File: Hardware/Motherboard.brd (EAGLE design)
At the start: 124.5 x 73.7 mm, 92 parts, among them J1 MICROMOD-2222-C, J10 MICRO-SD-PUSH-PUSH-EXT-PIN, J2 Vertical Qwiic Connector, J4 QWIIC_RIGHT_ANGLE, J5 CORTEX_JTAG_DEBUG_MINIMUM_PTH, J6 MICROMOD_CARRIER, J7 MICROMOD_CARRIER, Q1 3.1A/30V/105mΩ, U2 MCP73831, U5 AP7361C-33

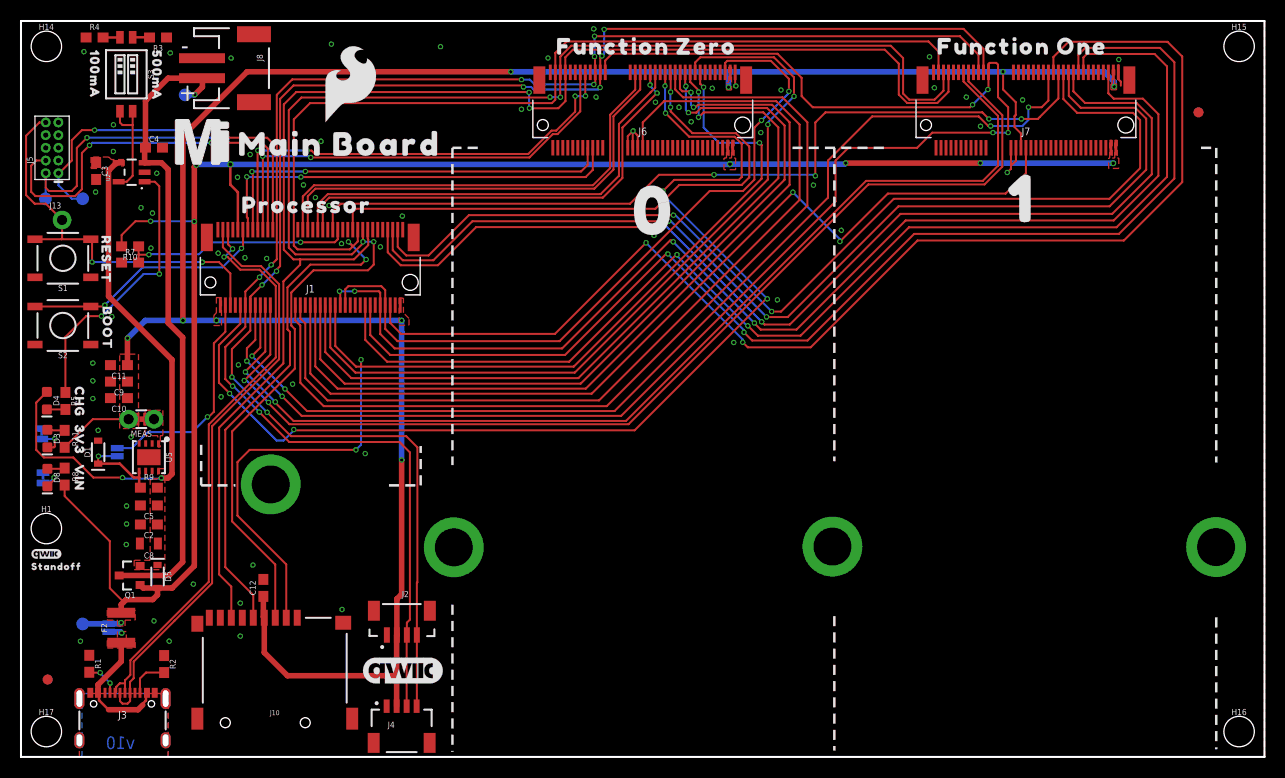
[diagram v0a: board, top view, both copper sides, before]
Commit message: Adds 10k pull down to PCHAN MOSFET
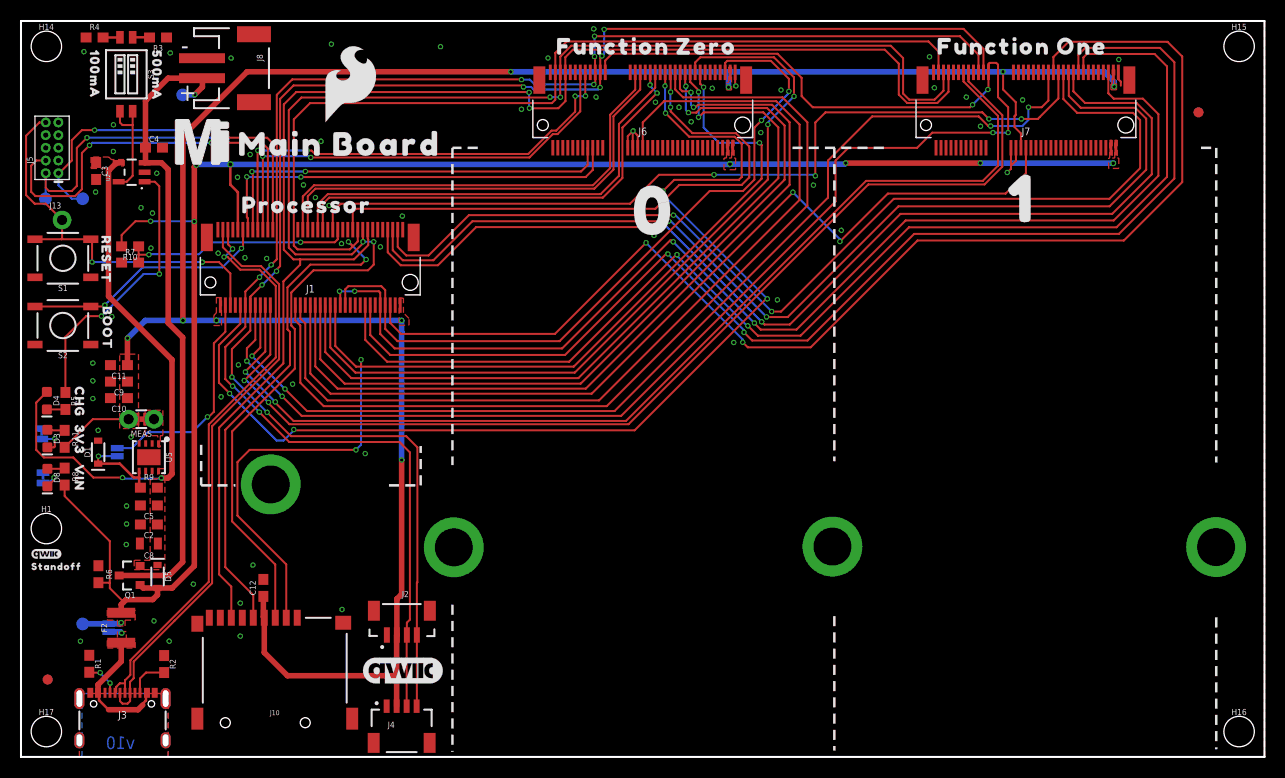
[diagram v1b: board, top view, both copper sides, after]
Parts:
- added R6: 10k, SparkFun-Resistors:0603
- moved TP3 0.25 mm to (16.2, 66.3)
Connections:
- net GND: now also R6.1
- net VIN: now also R6.2
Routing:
- net VIN: track 178.0 -> 179.2 mm
- net GND: track 13.7 -> 13.0 mm
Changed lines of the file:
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@@
 </element>
 <element name="TP2" library="SparkFun-Connectors" package="PAD.03X.05" value="TEST-POINT3X5" x="6.173" y="55.868" smashed="yes" rot="MR180"/>
-<element name="TP3" library="SparkFun-Connectors" package="PAD.03X.05" value="TEST-POINT3X5" x="16.4338" y="66.2686" smashed="yes" rot="MR270"/>
+<element name="TP3" library="SparkFun-Connectors" package="PAD.03X.05" value="TEST-POINT3X5" x="16.1798" y="66.2686" smashed="yes" rot="MR270"/>
 <element name="TP4" library="SparkFun-Connectors" package="PAD.03X.05" value="TEST-POINT3X5" x="6.1722" y="13.3096" smashed="yes" rot="MR0"/>
 <element name="TP1" library="SparkFun-Connectors" package="PAD.03X.05" value="TEST-POINT3X5" x="2.444" y="55.858" smashed="yes" rot="MR0"/>
@@
 <element name="U$23" library="top" package="STANDOFF501" value="" x="3.556" y="19.05" smashed="yes"/>
 <element name="U$24" library="SparkFun-Aesthetics" package="SFE_LOGO_FLAME_.3" value="" x="33.02" y="67.31" smashed="yes"/>
+<element name="R6" library="SparkFun-Resistors" package="0603" value="10k" x="7.747" y="18.288" smashed="yes" rot="R270">
+<attribute name="NAME" x="8.509" y="18.288" size="0.6096" layer="25" font="vector" ratio="20" rot="R270" align="bottom-center"/>
+<attribute name="PROD_ID" value="RES-00824" x="7.747" y="18.288" size="1.778" layer="27" font="vector" ratio="15" rot="R270" display="off"/>
+<attribute name="VALUE" x="6.985" y="18.288" size="0.6096" layer="27" font="vector" ratio="20" rot="R270" align="top-center"/>
+</element>
 </elements>
 <signals>
@@
 <via x="10.5664" y="23.3172" extent="1-16" drill="0.3048"/>
 <via x="10.541" y="21.2598" extent="1-16" drill="0.3048"/>
-<wire x1="109.834" y1="68.521" x2="109.834" y2="69.2448" width="0.2032" layer="1"/>
 <wire x1="109.834" y1="68.521" x2="109.834" y2="67.839" width="0.2032" layer="1"/>
 <wire x1="110.0836" y1="67.5894" x2="110.0836" y2="67.183" width="0.2032" layer="1"/>
@@
 <via x="13.3096" y="13.6144" extent="1-16" drill="0.3048"/>
 <via x="17.2466" y="17.2974" extent="1-16" drill="0.3048"/>
+<contactref element="R6" pad="1"/>
 </signal>
 <signal name="V_BATT" class="1">
@@
 <wire x1="16.1798" y1="41.9862" x2="14.732" y2="43.434" width="0.5588" layer="1"/>
 <wire x1="14.732" y1="43.434" x2="14.732" y2="58.801" width="0.5588" layer="1"/>
-<wire x1="12.3745" y1="59.4716" x2="12.3745" y2="60.8655" width="0.5588" layer="1"/>
 <wire x1="14.7226" y1="67.9356" x2="18.1186" y2="67.9356" width="0.5588" layer="1"/>
-<wire x1="12.4596" y1="60.9854" x2="12.4596" y2="65.6726" width="0.5588" layer="1"/>
-<wire x1="12.4596" y1="65.6726" x2="14.7226" y2="67.9356" width="0.5588" layer="1"/>
-<wire x1="16.4338" y1="66.2686" x2="17.3736" y2="66.2686" width="0.5588" layer="16"/>
+<wire x1="14.7226" y1="67.9356" x2="12.4596" y2="65.6726" width="0.5588" layer="1"/>
+<wire x1="16.1798" y1="66.2686" x2="17.3736" y2="66.2686" width="0.5588" layer="16"/>
 <wire x1="17.3736" y1="66.2686" x2="17.399" y2="66.294" width="0.5588" layer="16"/>
 <via x="17.399" y="66.294" extent="1-16" drill="0.3048"/>
@@
 <contactref element="Q1" pad="3"/>
 <wire x1="14.8336" y1="18.161" x2="9.822" y2="18.161" width="0.5588" layer="1"/>
-<wire x1="12.3745" y1="60.8655" x2="12.4596" y2="60.9854" width="0" layer="19" extent="1-1"/>
+<wire x1="12.4596" y1="65.6726" x2="12.4596" y2="60.9854" width="0.5588" layer="1"/>
+<wire x1="12.4596" y1="60.9854" x2="12.4596" y2="59.5567" width="0.5588" layer="1"/>
+<wire x1="12.4596" y1="59.5567" x2="12.3745" y2="59.4716" width="0.5588" layer="1"/>
 </signal>
 <signal name="N$14">
@@
 <wire x1="4.3688" y1="26.1112" x2="8.89" y2="21.59" width="0.2032" layer="1"/>
 <wire x1="8.89" y1="16.891" x2="10.2769" y2="15.5041" width="0.2032" layer="1"/>
-<wire x1="8.89" y1="21.59" x2="8.89" y2="16.891" width="0.2032" layer="1"/>
+<wire x1="8.89" y1="21.59" x2="8.89" y2="17.399" width="0.2032" layer="1"/>
 <contactref element="TP4" pad="1"/>
+<wire x1="8.89" y1="16.891" x2="8.89" y2="17.399" width="0.2032" layer="1"/>
 <wire x1="8.763" y1="13.335" x2="6.1976" y2="13.335" width="0.5588" layer="16"/>
 <wire x1="6.1976" y1="13.335" x2="6.1722" y2="13.3096" width="0.5588" layer="16"/>
@@
 <wire x1="13.6652" y1="16.9094" x2="12.2236" y2="16.9094" width="0.5588" layer="1"/>
 <wire x1="12.2236" y1="16.9094" x2="11.922" y2="17.211" width="0.5588" layer="1"/>
+<contactref element="R6" pad="2"/>
+<wire x1="7.747" y1="17.438" x2="8.851" y2="17.438" width="0.2032" layer="1"/>
+<wire x1="8.851" y1="17.438" x2="8.89" y2="17.399" width="0.2032" layer="1"/>
 </signal>
 <signal name="SHLD">

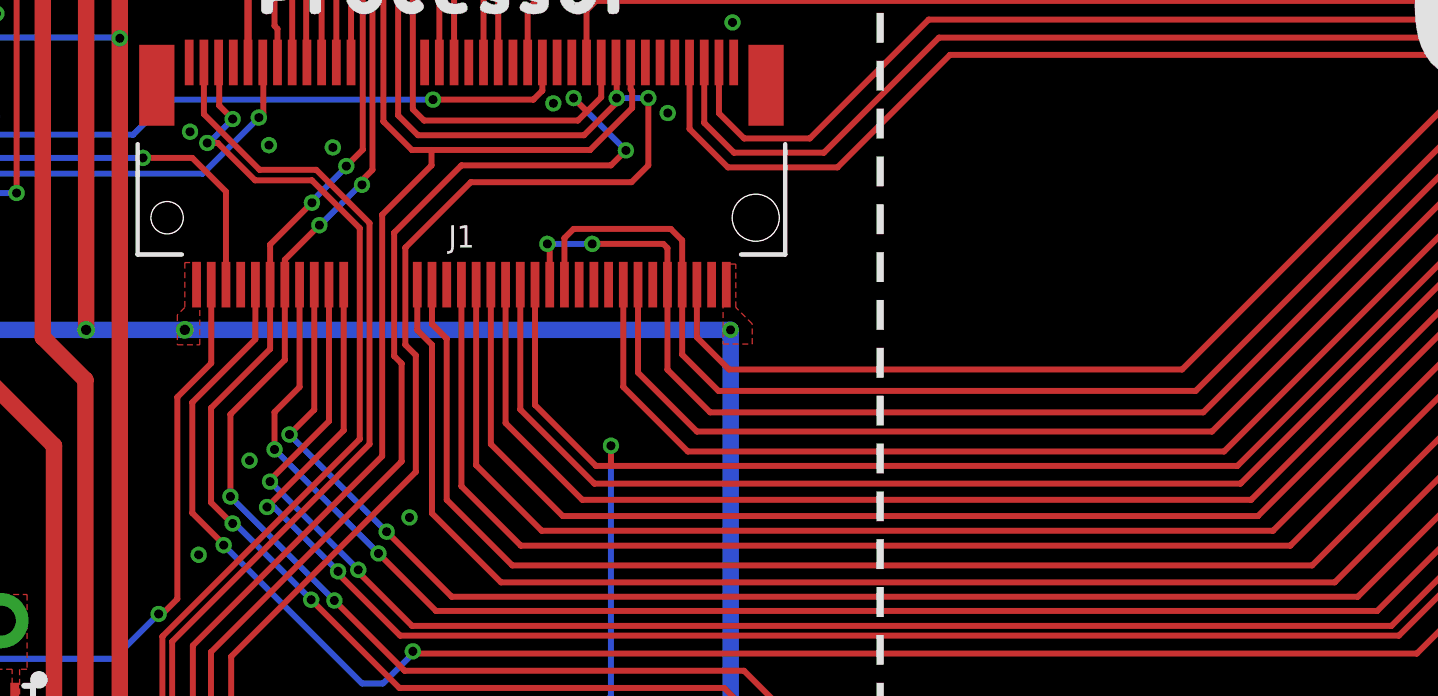
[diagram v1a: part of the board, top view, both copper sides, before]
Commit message: Adds jumpers to route power enable pins to G0/G1 for processors that don't have those nets routed
* Adds silk to added jumpers
* Adds PROD-ID to function board connectors
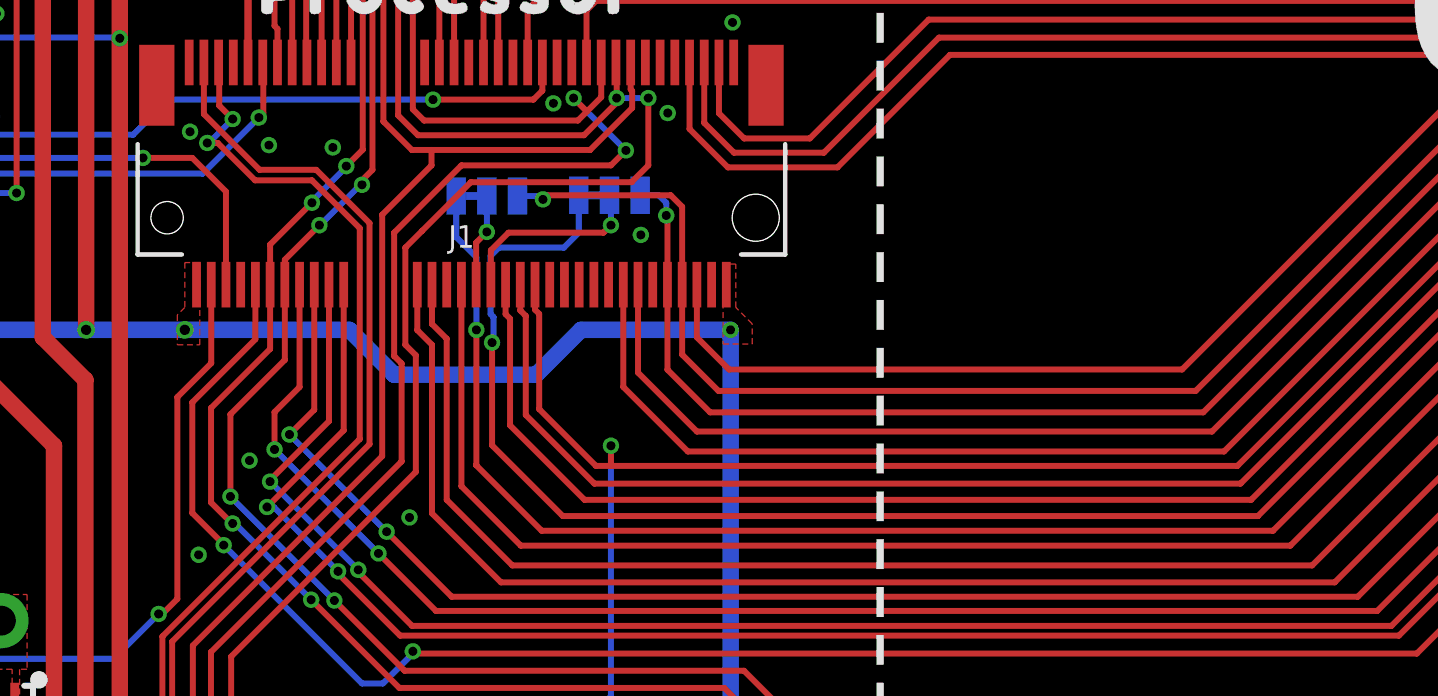
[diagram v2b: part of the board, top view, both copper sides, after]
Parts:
- added JP1, JP2: JUMPER-SMT_3_1-NC_TRACE_SILK, SparkFun-Jumpers:SMT-JUMPER_3_1-NC_TRACE_SILK
- added U$25: (no value), top:#G1#PROCESSOR#517
- added U$26: (no value), top:#G0#PROCESSOR#517
- added U$27: (no value), top:#ALT_PWR_EN1#517
- added U$28: (no value), top:#ALT_PWR_EN0#517
- H2, H3, H4, H8: value STAND-OFF-REFLOW2.5MM_TALL -> STAND-OFF-REFLOW-M2.5_2.5MM_TALL
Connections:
- new net G0-JUMPER: J1.40, JP2.2
- new net G1-JUMPER: J1.42, JP1.2
- net G0-PROCESSOR: now also JP2.3; no longer J1.40
- net G1-PROCESSOR: now also JP1.3; no longer J1.42
- net PWR_EN0: now also JP2.1; no longer J1.52
- net PWR_EN1: now also JP1.1; no longer J1.50
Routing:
- net G1-JUMPER: track 0.00 -> 6.64 mm, vias 0 -> 1
- net G1-PROCESSOR: track 81.5 -> 87.1 mm, vias 2 -> 3
- net G0-PROCESSOR: track 84.2 -> 87.9 mm, vias 2 -> 3
- net G0-JUMPER: track 0.00 -> 3.16 mm, vias 0 -> 1
- net PWR_EN1: track 116.9 -> 113.9 mm, vias 4 -> 3
- net 3.3V: track 242.4 -> 243.7 mm
- net PWR_EN0: track 73.6 -> 74.7 mm, vias 2 -> 3
- net GND: vias 72 -> 73

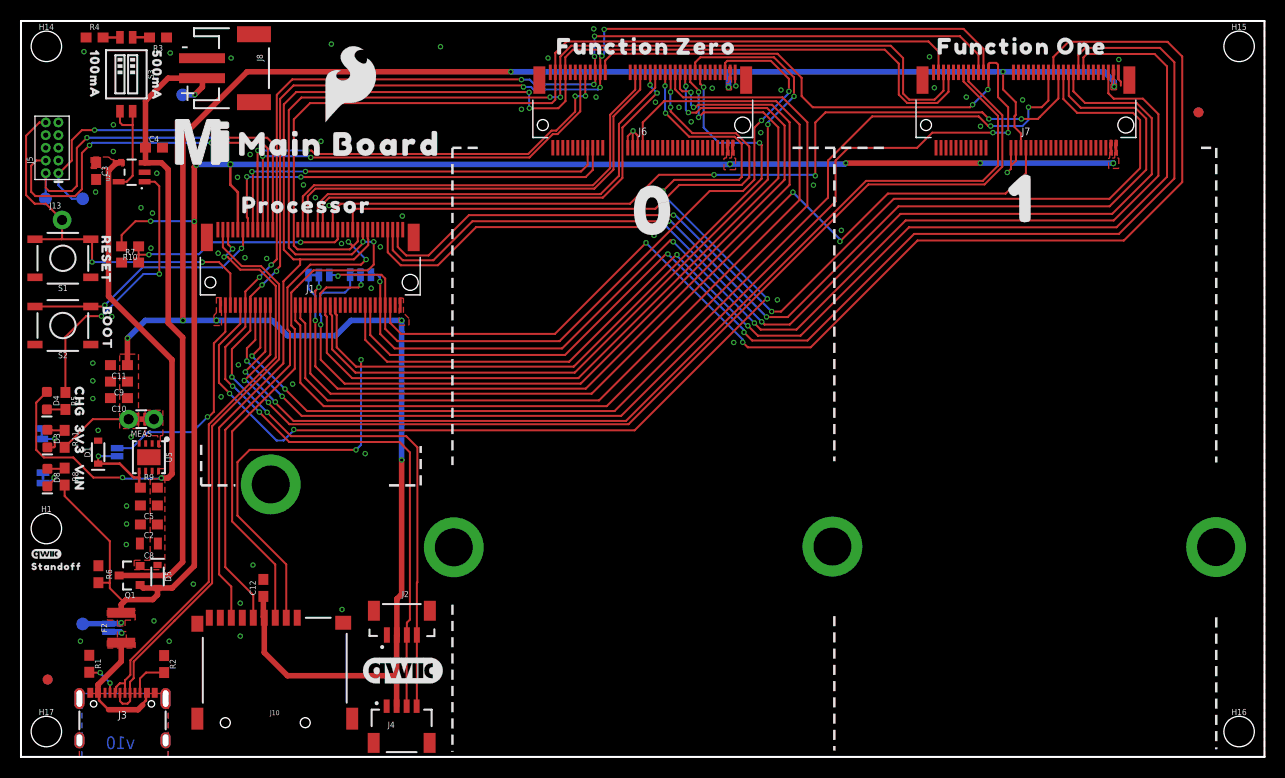
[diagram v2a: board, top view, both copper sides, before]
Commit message: Recreates changes from last change but instead moves jumpers to nets G5/G6
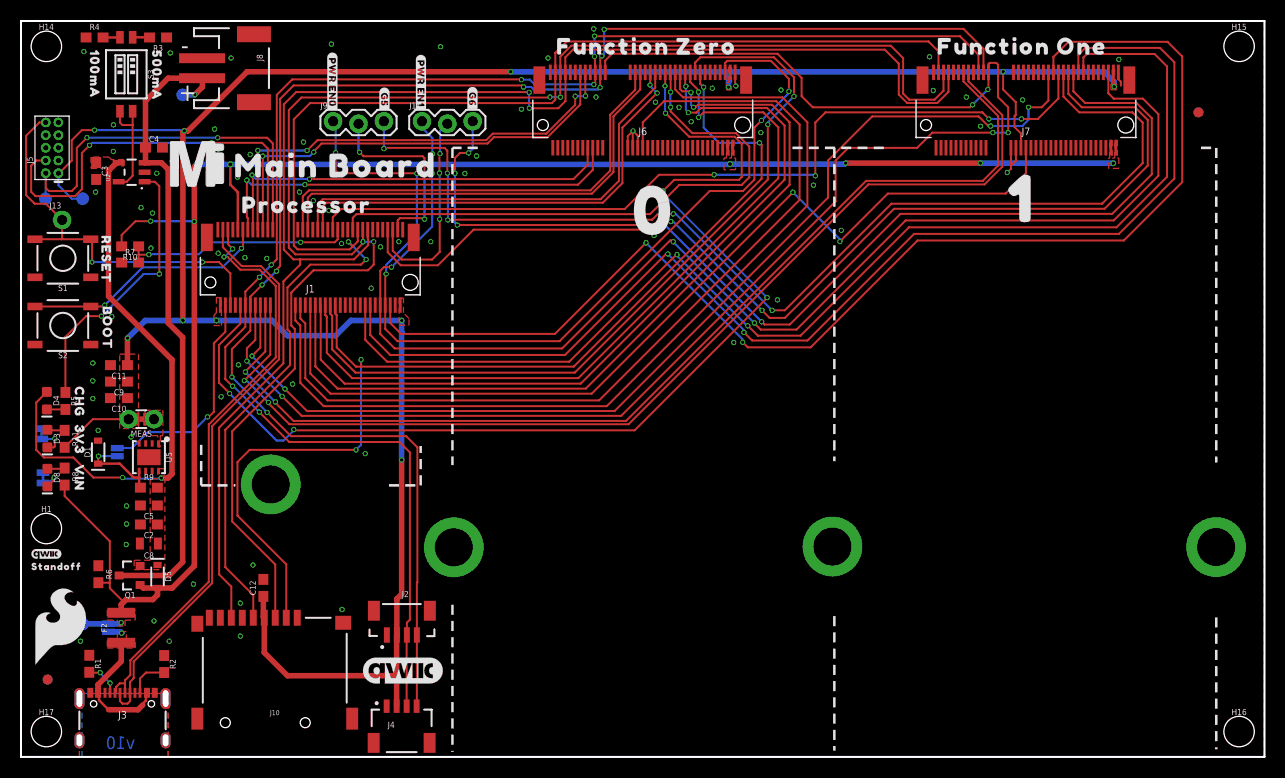
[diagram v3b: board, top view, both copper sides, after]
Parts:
- removed JP1, JP2: JUMPER-SMT_3_1-NC_TRACE_SILK, SparkFun-Jumpers:SMT-JUMPER_3_1-NC_TRACE_SILK
- added J11, J9: (no value), SparkFun-Connectors:1X03_LOCK
- added U$29: (no value), top:#G6#517
- added U$30: (no value), top:#PWR_EN0#517
- added U$31: (no value), top:#PWR_EN1#517
- added U$32: (no value), top:#G5#517
- moved U$24 61.6 mm to (3.99, 13.0)
- moved U$14 2.27 mm to (17.7, 59.4)
- moved U$21 2.19 mm to (31.5, 59.2)
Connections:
- removed net G0-JUMPER: J1.40, JP2.2
- removed net G1-JUMPER: J1.42, JP1.2
- new net G5-JUMPER: J1.73, J9.2
- new net G6-JUMPER: J1.71, J11.2
- net G0-PROCESSOR: now also J1.40; no longer JP2.3
- net G1-PROCESSOR: now also J1.42; no longer JP1.3
- net G5-PROCESSOR: now also J9.3; no longer J1.73
- net G6-PROCESSOR: now also J11.3; no longer J1.71
- net PWR_EN0: now also J9.1; no longer JP2.1
- net PWR_EN1: now also J11.1; no longer JP1.1
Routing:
- net G6-JUMPER: track 0.00 -> 20.6 mm, vias 0 -> 3
- net G5-JUMPER: track 0.00 -> 19.5 mm, vias 0 -> 3
- net PWR_EN0: track 74.7 -> 94.0 mm, vias 3 -> 5
- net PWR_EN1: track 113.9 -> 131.5 mm, vias 3 -> 5
- net G5-PROCESSOR: track 104.1 -> 111.6 mm, vias 2 -> 5
- net G1-JUMPER: track 6.64 -> 0.00 mm, vias 1 -> 0
- net G1-PROCESSOR: track 87.1 -> 81.5 mm, vias 3 -> 2
- net G0-PROCESSOR: track 87.9 -> 84.2 mm, vias 3 -> 2
- net G0-JUMPER: track 3.16 -> 0.00 mm, vias 1 -> 0
- net G6-PROCESSOR: track 105.8 -> 107.1 mm, vias 2 -> 5
- net TX1-PROCESSOR: track 46.6 -> 45.9 mm
- net GND: vias 73 -> 76
